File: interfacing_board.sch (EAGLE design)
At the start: 73 parts, among them IC1 AD817, IC2 AD817, IC3 AD817, IC4 AD817, IC5 AD817, IC8 AD817, X1 87758-3816, X2 87758-3816, X4 22-23-2081

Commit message: Rev1.9. Small board, autorouted. Too thin routes. For SED2.0
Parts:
- removed ALBIN1, ALBIN2: 22-05-7028-02, EP_molex_6410_7395:22-05-7028-02
- removed C7, C8: 0.1uF, capacitor-wima:C2.5/2
- removed IC1, IC2, IC3, IC4, IC5, IC8: AD817, analog-devices:AD817
- removed OPTO2, OPTO3, OPTO4: 332-04, con-garry:332-04
- removed R24, R30, R33: 1k, eagle-ltspice:R0207/10
- removed R26, R31, R34: 10k, eagle-ltspice:R0207/10
- removed R29, R32, R7: 100, eagle-ltspice:R0207/10
- added ALB1, ALB2: 22-05-7028-02, EP_molex_6410_7395:22-05-7028-02
- added C3, C4: 0.1uF, capacitor-wima:C2.5/2
- added IC10, IC11, IC12, IC6, IC7, IC9: AD817, analog-devices:AD817
- added LEVEL_TRANSLATOR: 74LVC8T245, 74lvc8t245:74LVC8T245
- added OPTO5, OPTO6, OPTO7: 332-04, con-garry:332-04
- added R1, R2, R3, R39, R4, R40, R41, R42, R43, R44, R45, R46, R47, R48, R49, R50, R51, R52, R53, R54, R55, R56, R57, R58: (no value), adafruit:R-US_M0805
- added R59: 2k, eagle-ltspice:R0207/10
- added R60, R61, R62, R63, R64, R65, R66, R67: (no value), resistor:R-EU_M0805
- added U$3, U$4, U$5, U$6, U$7: LMC6001, customy:LMC6001
- R23: value 2k -> (none); device eagle-ltspice:R0207/10 -> resistor:R-EU_M0805
- R25: value 10k -> (none); device eagle-ltspice:R0207/10 -> resistor:R-EU_M0805
- R5: value 100 -> (none); device eagle-ltspice:R0207/10 -> resistor:R-EU_M0805
- R6: value 1k -> (none); device eagle-ltspice:R0207/10 -> resistor:R-EU_M0805
- U$2: value 74LVC8T245 -> LMC6001; device 74lvc8t245:74LVC8T245 -> customy:LMC6001
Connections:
- net N$24 renamed OL-GRN
- net N$25 renamed OL-BLK
- net N$26 renamed ADC-ADDR
- net N$31 renamed ADC-ALRT
- net N$33 renamed DRV1-VM
- net N$56 renamed DRV2-VM
- net PC1 renamed ADC12_IN9
- removed net EMPTY: ETHER-3.S
- removed net EXTADC0: ADCA0.S
- removed net EXTADC1: ADCA1.S
- removed net EXTADC2: ADCA2.S
- removed net EXTADC3: ADCA3.S
- removed net M1PWM: X2-37.S
- removed net M2PWM: X2-38.S
- removed net N$13: OPTO2-1.S, R7.1
- removed net N$14: OPTO2-2.S, R24.1
- removed net N$17: OPTO3-1.S, R29.1
- removed net N$18: OPTO3-2.S, R30.1
- removed net N$21: OPTO4-1.S, R32.1
- removed net N$22: OPTO4-2.S, R33.1
- removed net N$27: ADCSDA.S
- removed net N$28: ADCSCL.S
- removed net N$38: ENDR1-5.S
- removed net N$40: ENDR1-9.S
- removed net N$42: ENDR1-4.S
- removed net N$43: ENDR1-6.S
- removed net N$44: ENDR1-8.S
- removed net N$45: ENDR1-10.S
- removed net N$46: ENDR2-1.S
- removed net N$47: ENDR2-3.S
- removed net N$48: ENDR2-5.S
- removed net N$49: ENDR2-7.S
- removed net N$50: ENDR2-9.S
- removed net N$51: ENDR2-2.S
- removed net N$52: ENDR2-4.S
- removed net N$53: ENDR2-6.S
- removed net N$54: ENDR2-8.S
- removed net N$55: ENDR2-10.S
- removed net PA0: X1-11.S
- removed net PA1: X1-9.S
- removed net PA10: X2-6.S
- removed net PA9: X2-18.S
- removed net PB10: X2-14.S
- removed net PB11: X2-21.S
- removed net PB6: X2-22.S
- removed net PB7: X1-18.S
- new net ADC-SCL: ADCSCL.S, X1-18.S
- new net ADC-SDA: ADCSDA.S, X2-22.S
- new net ADC12_IN8: X1-5.S
- new net CHA-1: IC7.OUT, LEVEL_TRANSLATOR.B1, R41.1
- new net CHA-1L: LEVEL_TRANSLATOR.A1
- new net CHA-2: IC11.OUT, LEVEL_TRANSLATOR.B4, R53.1
- new net CHA-2L: LEVEL_TRANSLATOR.A4, X1-9.S
- new net CHB-1: IC6.OUT, LEVEL_TRANSLATOR.B2, R3.1
- new net CHB-1L: LEVEL_TRANSLATOR.A2
- new net CHB-2: IC10.OUT, LEVEL_TRANSLATOR.B5, R49.1
- new net CHB-2L: LEVEL_TRANSLATOR.A5, X2-14.S
- new net CHC-1: IC9.OUT, LEVEL_TRANSLATOR.B3, R45.1
- new net CHC-1L: LEVEL_TRANSLATOR.A3, X1-11.S
- new net CHC-2: IC12.OUT, LEVEL_TRANSLATOR.B6, R57.1
- new net CHC-2L: LEVEL_TRANSLATOR.A6, X2-21.S
- new net INCHA-1: ENDR1-6.S, R40.1
- new net INCHA-2: ENDR2-6.S, R52.1
- new net INCHB-1: ENDR1-8.S, R1.1
- new net INCHB-2: ENDR2-8.S, R47.1
- new net INCHC-1: ENDR1-10.S, R43.1
- new net INCHC-2: ENDR2-10.S, R55.1
- new net IND3: OPTO5-1.S, R61.2
- new net IND4: OPTO7-1.S, R67.2
- new net N$1: IC6.IN-, R1.2, R3.2
- new net N$10: IC10.IN+, R48.2, R50.1
- new net N$15: OPTO6-4.S, R62.1
- new net N$19: IC11.IN-, R51.2, R53.2
- new net N$20: IC7.IN-, R39.2, R41.2
- new net N$29: C3.1, R59.2, U$2.N, UV1-2.S
- new net N$30: IC7.IN+, R40.2, R42.1
- new net N$32: IC9.IN-, R43.2, R45.2
- new net N$34: IC9.IN+, R44.2, R46.1
- new net N$35: IC11.IN+, R52.2, R54.1
- new net N$4: IC6.IN+, R2.2, R4.1
- new net N$9: IC10.IN-, R47.2, R49.2
- new net OL_RX: OPENLOGRXI.1, X2-18.S
- new net OL_TX: OPENLOGTXO.1, X2-6.S
- new net ~INCHA-1: ENDR1-5.S, R39.1
- new net ~INCHA-2: ENDR2-5.S, R51.1
- new net ~INCHB-1: ENDR1-7.S, R2.1
- new net ~INCHB-2: ENDR2-7.S, R48.1
- new net ~INCHC-1: ENDR1-9.S, R44.1
- new net ~INCHC-2: ENDR2-9.S, R56.1
- net 3.3V: now also LEVEL_TRANSLATOR.VCCA, R25.2, R60.2, R62.2, R63.2, R65.2, R66.2, U$2.VDD, U$3.VDD, U$4.VDD, U$5.VDD, U$6.VDD, U$7.VDD; no longer IC1.+VS, IC2.+VS, IC3.+VS, IC4.+VS, IC5.+VS, IC8.+VS, R24.2, R29.2, R30.2, R32.2, R33.2, R7.2
- net 5V: now also ENDR1-2.S, ENDR2-2.S, IC10.+VS, IC11.+VS, IC12.+VS, IC6.+VS, IC7.+VS, IC9.+VS, LEVEL_TRANSLATOR.VCCB, LEVEL_TRANSLATOR.VCCB2
- net ALBEDO1: now also C5.2, C6.2, R21.1, R22.1, U$6.VOUT, U$7.VOUT, X2-5.S; no longer C1.2, IC5.OUT, R16.1
- net ALBEDO2: now also X2-33.S; no longer C2.2, IC8.OUT, R17.1
- net CS_HTP2: now also X2-37.S
- net CS_RTC: now also X2-38.S
- net GND: now also ALB1-1.S, ALB2-1.S, ENDR1-3.S, ENDR2-3.S, IC10.-VS, IC11.-VS, IC12.-VS, IC6.-VS, IC7.-VS, IC9.-VS, LEVEL_TRANSLATOR.DIR, LEVEL_TRANSLATOR.GND, LEVEL_TRANSLATOR.GND2, LEVEL_TRANSLATOR.GND3, LEVEL_TRANSLATOR.OE, OPTO1-2.S, OPTO5-2.S, OPTO6-2.S, OPTO7-2.S, R23.1, R4.2, R42.2, R46.2, R50.2, R54.2, R58.2, R61.1, R64.1, R67.1, U$2.P, U$2.VSS, U$3.P, U$3.VSS, U$4.P, U$4.VSS, U$5.P, U$5.VSS, U$6.P, U$6.VSS, U$7.P, U$7.VSS, UV1-1.S, UV2-1.S, VIS1-1.S, VIS2-1.S; no longer ALBIN1-2.S, ALBIN2-2.S, IC1.-VS, IC1.IN+, IC1.OFF@2, IC2.-VS, IC2.IN+, IC2.OFF@2, IC3.-VS, IC3.IN+, IC3.OFF@2, IC4.-VS, IC4.IN+, IC4.OFF@2, IC5.-VS, IC5.IN+, IC5.OFF@2, IC8.-VS, IC8.IN+, IC8.OFF@2, OPTO1-3.S, OPTO2-3.S, OPTO3-3.S, OPTO4-3.S, R25.2, R26.2, R31.2, R34.2, UV1-2.S, UV2-2.S, VIS1-2.S, VIS2-2.S
- net IND1: now also OPTO1-1.S, R23.2; no longer OPTO1-4.S, OPTO3-4.S, R25.1, R31.1
- net IND2: now also OPTO6-1.S, R64.2; no longer OPTO2-4.S, OPTO4-4.S, R26.1, R34.1
- net N$11: now also OPTO5-4.S, R25.1; no longer OPTO1-1.S, R5.1
- net N$12: now also OPTO6-3.S, R63.1; no longer OPTO1-2.S, R6.1
- net N$16: now also OPTO7-3.S, R66.1; no longer OPENLOGTXO.1
- net N$2: now also OPTO1-3.S, R6.1; no longer ALBIN1-1.S, C1.1, IC5.IN-, R16.2
- net N$23: now also OPTO7-4.S, R65.1; no longer OPENLOGRXI.1
- net N$3: now also C1.1, R16.2, U$3.N, UV2-2.S; no longer ALBIN2-1.S, C2.1, IC8.IN-, R17.2
- net N$36: now also IC12.IN-, R55.2, R57.2; no longer ENDR1-1.S
- net N$37: now also IC12.IN+, R56.2, R58.1; no longer ENDR1-3.S
- net N$39: now also ALB1-2.S, C5.1, R21.2, U$6.N; no longer ENDR1-7.S
- net N$41: now also ALB2-2.S, C6.1, R22.2, U$7.N; no longer ENDR1-2.S
- net N$5: now also OPTO5-3.S, R60.1; no longer C6.1, IC1.IN-, R21.2, VIS1-1.S
- net N$6: now also C2.1, R17.2, U$4.N, VIS1-2.S; no longer C7.1, IC3.IN-, R22.2, UV2-1.S
- net N$7: now also OPTO1-4.S, R5.1; no longer C8.1, IC4.IN-, R23.2, VIS2-1.S
- net N$8: now also C4.1, U$5.N, VIS2-2.S; no longer C5.1, IC2.IN-, UV1-1.S
- net UV1: now also ADCA0.S, C3.2, R59.1, U$2.VOUT; no longer C5.2, IC2.OUT, R20.1, X2-5.S
- net UV2: now also ADCA1.S, C1.2, R16.1, U$3.VOUT; no longer C7.2, IC3.OUT, R22.1, X2-33.S
- net VIS1: now also ADCA2.S, C2.2, R17.1, U$4.VOUT; no longer C6.2, IC1.OUT, R21.1, X1-5.S
- net VIS2: now also ADCA3.S, C4.2, R20.1, U$5.VOUT; no longer C8.2, IC4.OUT, R23.1
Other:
- note added: "14.05.2018"
- note added: "Board for Interfacing Peripherals and OBC"
- note added: "Differential amplifiers"
- note added: "LUSTRO - BIPOP"
- note added: "Level translator 5V -> 3.3V"
- note added: "UV sensors"
- note added: "Vis sensors"
- note removed: "11.05.2018"
- note removed: "Board for Interfacing Peripherals and OBC (BIPOP)"
- note removed: "CS_HTP2"
- note removed: "CS_SD"
- note removed: "Connect:"
- note removed: "LUSTRO"
- note removed: "M1PWM"
- note removed: "M2PWM"
- note removed: "OpenLog"
- note removed: "UV&Vis sensors"
- note removed: "add differential amplifiers for encoders"
- note removed: "add voltage shifters for encoders"
- note removed: "adjust the operational amplifiers"
- note removed: "encoders"
- note removed: "extADC"
- note removed: "remove connections:"
- note removed: "update"
- moved on the sheet: ADCA0, ADCA1, ADCA2, ADCA3, ADCADDR, ADCALRT, ADCGND, ADCSCL, ADCSDA, ADCVDD, C1, C2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

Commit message: deleted photodiode sockets and their amplifiers on interfacing board schematic and PCB
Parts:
- removed ADC: ADS1015, SKA_EP_molex_6410_7395:ADS1015
- removed ALB1, ALB2, UV1, UV2, VIS1, VIS2: 22-05-7028-02, EP_molex_6410_7395:22-05-7028-02
- removed C1, C2, C3, C4, C5, C6: 0.1uF, capacitor-wima:C2.5/2
- removed R16, R17, R20, R21, R22, R59: 2k, eagle-ltspice:R0207/10
- removed U$2, U$3, U$4, U$5, U$6, U$7: LMC6001, customy:LMC6001
- added J1: 22-05-7048-04, EP_molex_6410_7395:22-05-7048-04
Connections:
- net ALBEDO2 renamed PC5
- removed net ADC-ADDR: ADCADDR.1
- removed net ADC-ALRT: ADCALRT.S
- removed net ADC-SCL: ADCSCL.S, X1-18.S
- removed net ADC-SDA: ADCSDA.S, X2-22.S
- removed net ALBEDO1: C5.2, C6.2, R21.1, R22.1, U$6.VOUT, U$7.VOUT, X2-5.S
- removed net N$29: C3.1, R59.2, U$2.N, UV1-2.S
- removed net N$3: C1.1, R16.2, U$3.N, UV2-2.S
- removed net N$39: ALB1-2.S, C5.1, R21.2, U$6.N
- removed net N$41: ALB2-2.S, C6.1, R22.2, U$7.N
- removed net N$6: C2.1, R17.2, U$4.N, VIS1-2.S
- removed net N$8: C4.1, R20.2, U$5.N, VIS2-2.S
- removed net UV1: ADCA0.S, C3.2, R59.1, U$2.VOUT
- removed net UV2: ADCA1.S, C1.2, R16.1, U$3.VOUT
- removed net VIS1: ADCA2.S, C2.2, R17.1, U$4.VOUT
- removed net VIS2: ADCA3.S, C4.2, R20.1, U$5.VOUT, X2-15.S
- new net PC4: X2-5.S
- new net SCL1: X2-22.S
- new net SDA1: X1-18.S
- new net VIS2<<<<<<<<<<: X2-15.S
- net 3.3V: no longer ADCVDD.S, U$2.VDD, U$3.VDD, U$4.VDD, U$5.VDD, U$6.VDD, U$7.VDD
- net GND: no longer ADCGND.S, ALB1-1.S, ALB2-1.S, U$2.P, U$2.VSS, U$3.P, U$3.VSS, U$4.P, U$4.VSS, U$5.P, U$5.VSS, U$6.P, U$6.VSS, U$7.P, U$7.VSS, UV1-1.S, UV2-1.S, VIS1-1.S, VIS2-1.S
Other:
- note removed: "Albedo sensors"
- note removed: "External ADC"
- note removed: "Vis sensors"

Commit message: updated pullups
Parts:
- removed IC10, IC11, IC12, IC6, IC7, IC9: AD817, analog-devices:AD817
- removed J1: 22-05-7048-04, EP_molex_6410_7395:22-05-7048-04
- removed LEVEL_TRANSLATOR: 74LVC8T245, 74lvc8t245:74LVC8T245
- removed R28, R35, R36, R37, R38: 2k, eagle-ltspice:R0207/10
- removed R39, R40, R41, R42, R43, R44, R45, R46, R47, R48, R49, R50, R51, R52, R53, R54, R55, R56, R57, R58: (no value), adafruit:R-US_M0805
- added ALBEDO1, ALBEDO2, UV1, UV2, VIS1, VIS2: 22-05-7048-04, EP_molex_6410_7395:22-05-7048-04
- added IC1, IC2: MAX3096CSE, maxim:MAX3096CSE
- added R16, R20, R22, R26, R30, R32: 10k, rcl:R-EU_M0805
- added R17, R21, R24, R29, R31, R7: 5k, rcl:R-EU_M0805
- R1, R2, R3, R4: value (none) -> 10k; device adafruit:R-US_M0805 -> rcl:R-EU_M0805
- R10, R11, R8, R9: value 2k -> 4.7k; device eagle-ltspice:R0207/10 -> rcl:R-EU_M0805
- R12, R13, R14, R15, R19, R27: value 2k -> 5k; device eagle-ltspice:R0207/10 -> rcl:R-EU_M0805
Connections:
- removed net N$1: IC6.IN-, R1.2, R3.2
- removed net N$10: IC10.IN+, R48.2, R50.1
- removed net N$20: IC7.IN-, R39.2, R41.2
- removed net N$30: IC7.IN+, R40.2, R42.1
- removed net N$32: IC9.IN-, R43.2, R45.2
- removed net N$34: IC9.IN+, R44.2, R46.1
- removed net N$35: IC11.IN+, R52.2, R54.1
- removed net N$36: IC12.IN-, R55.2, R57.2
- removed net N$37: IC12.IN+, R56.2, R58.1
- removed net N$4: IC6.IN+, R2.2, R4.1
- removed net N$9: IC10.IN-, R47.2, R49.2
- new net CHB2-L: R29.1, R30.2
- new net N$13: IC2.!G, R4.1
- new net N$18: IC1.G, R1.2
- new net N$8: IC2.G, R3.2
- new net SCL2: VIS1-3.S, VIS2-3.S
- new net SDA2: VIS1-2.S, VIS2-2.S
- net +5V: now also R1.1, R3.1
- net 3.3V: now also ALBEDO1-1.S, ALBEDO2-1.S, UV1-1.S, UV2-1.S, VIS1-1.S, VIS2-1.S; no longer LEVEL_TRANSLATOR.VCCA, R28.2, R35.2, R36.2, R37.2, R38.2
- net 5V: now also IC1.VCC, IC2.VCC; no longer IC10.+VS, IC11.+VS, IC12.+VS, IC6.+VS, IC7.+VS, IC9.+VS, LEVEL_TRANSLATOR.VCCB, LEVEL_TRANSLATOR.VCCB2
- net CHA-1: now also IC1.Y1, R7.2; no longer IC7.OUT, LEVEL_TRANSLATOR.B1, R41.1
- net CHA-1L: now also R16.2, R7.1; no longer LEVEL_TRANSLATOR.A1
- net CHA-2: now also IC2.Y1, R24.2; no longer IC11.OUT, LEVEL_TRANSLATOR.B4, R53.1
- net CHA-2L: now also R24.1, R26.2; no longer LEVEL_TRANSLATOR.A4
- net CHB-1: now also IC1.Y2, R17.2; no longer IC6.OUT, LEVEL_TRANSLATOR.B2, R3.1
- net CHB-1L: now also R17.1, R20.2; no longer LEVEL_TRANSLATOR.A2
- net CHB-2: now also IC2.Y2, R29.2; no longer IC10.OUT, LEVEL_TRANSLATOR.B5, R49.1
- net CHB-2L: no longer LEVEL_TRANSLATOR.A5
- net CHC-1: now also IC1.Y3, R21.2; no longer IC9.OUT, LEVEL_TRANSLATOR.B3, R45.1
- net CHC-1L: now also R21.1, R22.2; no longer LEVEL_TRANSLATOR.A3
- net CHC-2: now also IC2.Y3, R31.2; no longer IC12.OUT, LEVEL_TRANSLATOR.B6, R57.1
- net CHC-2L: now also R31.1, R32.2; no longer LEVEL_TRANSLATOR.A6
- net CS_HTP: no longer R12.1
- net CS_HTP2: no longer R35.1
- net CS_IMU: no longer R8.1
- net GND: now also ALBEDO1-4.S, ALBEDO2-4.S, IC1.GND, IC2.GND, R16.1, R2.2, R20.1, R22.1, R26.1, R30.1, R32.1, UV1-4.S, UV2-4.S, VIS1-4.S, VIS2-4.S; no longer IC10.-VS, IC11.-VS, IC12.-VS, IC6.-VS, IC7.-VS, IC9.-VS, LEVEL_TRANSLATOR.DIR, LEVEL_TRANSLATOR.GND, LEVEL_TRANSLATOR.GND2, LEVEL_TRANSLATOR.GND3, LEVEL_TRANSLATOR.OE, R42.2, R46.2, R50.2, R54.2, R58.2
- net INCHA-1: now also IC1.A1; no longer R40.1
- net INCHA-2: now also IC2.A1; no longer R52.1
- net INCHB-1: now also IC1.A2; no longer R1.1
- net INCHB-2: now also IC2.A2; no longer R47.1
- net INCHC-1: now also IC1.A3; no longer R43.1
- net INCHC-2: now also IC2.A3; no longer R55.1
- net N$19: now also IC1.!G, R2.1; no longer IC11.IN-, R51.2, R53.2
- net SCL1: now also ALBEDO1-3.S, ALBEDO2-3.S, R11.1, UV1-3.S, UV2-3.S
- net SDA1: now also ALBEDO1-2.S, ALBEDO2-2.S, R10.1, UV1-2.S, UV2-2.S
- net SPI1_MISO: now also R13.1
- net SPI1_MOSI: now also R12.1
- net SPI1_SCK: now also R14.1
- net SPI2_MISO: now also R19.1; no longer R11.1, R14.1, R28.1, R37.1
- net SPI2_MOSI: now also R15.1; no longer R10.1, R13.1, R27.1, R36.1
- net SPI2_SCK: now also R27.1; no longer R15.1, R19.1, R38.1, R9.1
- net ~INCHA-1: now also IC1.B1; no longer R39.1
- net ~INCHA-2: now also IC2.B1; no longer R51.1
- net ~INCHB-1: now also IC1.B2; no longer R2.1
- net ~INCHB-2: now also IC2.B2; no longer R48.1
- net ~INCHC-1: now also IC1.B3; no longer R44.1
- net ~INCHC-2: now also IC2.B3; no longer R56.1
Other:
- note added: "<<<<<<<<<<<<< <<<<<<<<<<<<< <<<<<<<<<<<<<"
- moved on the sheet: DRIVER1-GND, DRIVER1-IN1, DRIVER1-IN2, DRIVER1-VM, DRIVER2-GND, DRIVER2-IN1, DRIVER2-IN2, DRIVER2-VM, ENDR1-1, ENDR1-10, ENDR1-2, ENDR1-3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

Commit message: BIPOP updated. Grid errors corrected, pull-ups for CS pins added.
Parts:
- removed HTP: 22-05-7078-07, EP_molex_6410_7395:22-05-7078-07
- removed R8: 4.7k, rcl:R-EU_M0805
- removed U$1: RTC_WAVESHARE, SKA_EP_molex_6410_7395:RTC_WAVESHARE
- removed X4: 22-23-2081, con-molex:22-23-2081
- added HTP2: 22-27-2071-07, EP_molex_6410_7395:22-27-2071-07
- added IMU: 22-27-2081-08, EP_molex_6410_7395:22-27-2081-08
- added R28, R33: 4.7k, rcl:R-EU_M0805
- added RTC_: RTC_WAVESHARE, SKA_EP_molex_6410_7395:RTC_WAVESHARE
- HTP1: value 22-05-7078-07 -> 22-27-2071-07; device EP_molex_6410_7395:22-05-7078-07 -> EP_molex_6410_7395:22-27-2071-07
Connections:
- net VIS2<<<<<<<<<< renamed PB1
- net 3.3V: now also HTP2-7.S, IMU-7.S, R28.2, R33.2, RTC_RTCVCC.1; no longer HTP-7.S, R8.2, U$1RTCVCC.1, X4-7.S
- net 3V_O: now also HTP1-6.S; no longer HTP-6.S
- net 3V_O2: now also HTP2-6.S; no longer HTP1-6.S
- net CS_HTP: now also HTP1-1.S, R9.1; no longer HTP-1.S
- net CS_HTP2: now also HTP2-1.S, R28.1; no longer HTP1-1.S
- net CS_IMU: now also IMU-1.S, R33.1; no longer X4-1.S
- net CS_RTC: now also RTC_RTCCS.1; no longer U$1RTCCS.1
- net GND: now also HTP2-5.S, IMU-5.S, IMU-8.S, RTC_RTCGND.1; no longer HTP-5.S, U$1RTCGND.1, X4-5.S, X4-8.S
- net IMU_INT: now also IMU-6.S; no longer X4-6.S
- net SPI2_MISO: now also HTP2-3.S, IMU-4.S, RTC_RTCMISO.1; no longer HTP-3.S, U$1RTCMISO.1, X4-4.S
- net SPI2_MOSI: now also HTP2-2.S, IMU-3.S, RTC_RTCMOSI.1; no longer HTP-2.S, U$1RTCMOSI.1, X4-3.S
- net SPI2_SCK: now also HTP2-4.S, IMU-2.S, RTC_RTCSCK.1; no longer HTP-4.S, U$1RTCSCK.1, X4-2.S
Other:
- note added: "RS-422 encoder receivers"
- note removed: "<<<<<<<<<<<<< <<<<<<<<<<<<< <<<<<<<<<<<<<"
- note removed: "Differential amplifiers"
- note removed: "FSYNC"
- moved on the sheet: HTP1-1, HTP1-2, HTP1-3, HTP1-4, HTP1-5, HTP1-6, HTP1-7, R10, R11, R12, R13, R14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

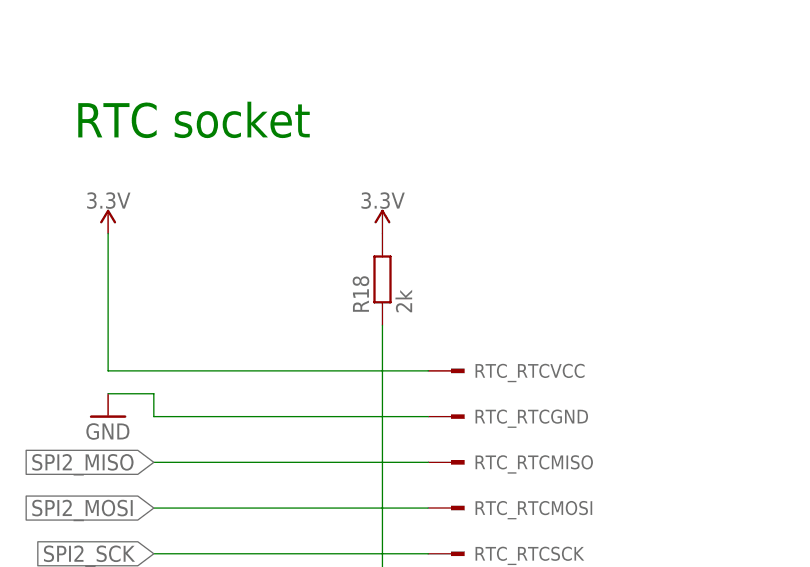
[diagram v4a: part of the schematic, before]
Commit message: Autorouter on BIPOP board.
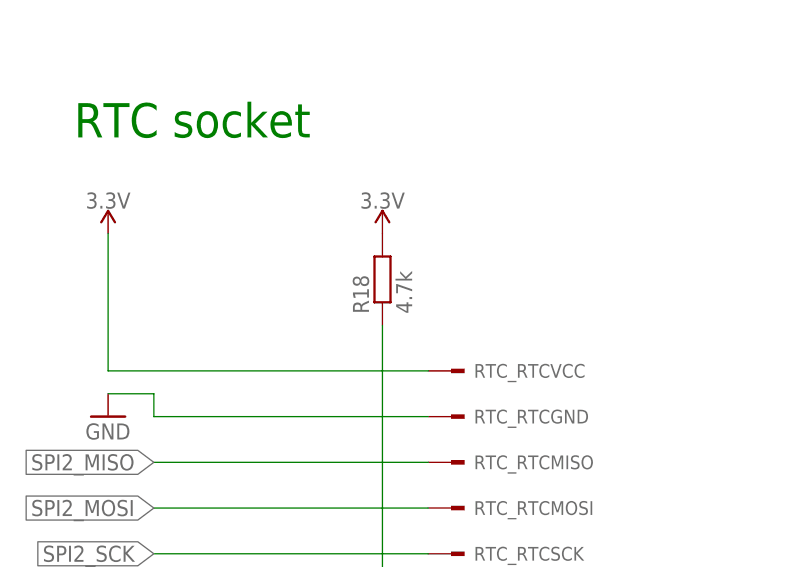
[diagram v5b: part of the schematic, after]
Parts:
- R18: value 2k -> 4.7k; device eagle-ltspice:R0207/10 -> rcl:R-EU_R0805
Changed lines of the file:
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@@
 <setting verticaltext="up"/>
 </settings>
-<grid distance="0.1" unitdist="inch" unit="inch" style="lines" multiple="1" display="yes" altdistance="0.01" altunitdist="inch" altunit="inch"/>
+<grid distance="0.1" unitdist="inch" unit="inch" style="lines" multiple="1" display="no" altdistance="0.01" altunitdist="inch" altunit="inch"/>
 <layers>
 <layer number="1" name="Top" color="4" fill="10" visible="no" active="no"/>
@@
 <part name="SUPPLY1" library="SparkFun-PowerSymbols" library_urn="urn:adsk.eagle:library:530" deviceset="3.3V" device=""/>
 <part name="SUPPLY5" library="SparkFun-PowerSymbols" library_urn="urn:adsk.eagle:library:530" deviceset="5V" device=""/>
-<part name="R18" library="eagle-ltspice" library_urn="urn:adsk.eagle:library:217" deviceset="R" device="0207/10" package3d_urn="urn:adsk.eagle:package:13275/1" value="2k"/>
+<part name="R18" library="rcl" library_urn="urn:adsk.eagle:library:334" deviceset="R-EU_" device="R0805" package3d_urn="urn:adsk.eagle:package:23553/2" value="4.7k"/>
 <part name="SUPPLY39" library="SparkFun-PowerSymbols" library_urn="urn:adsk.eagle:library:530" deviceset="3.3V" device=""/>
 <part name="GND4" library="supply1" library_urn="urn:adsk.eagle:library:371" deviceset="GND" device=""/>
